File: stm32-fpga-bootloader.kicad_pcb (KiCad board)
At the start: 4 copper layers, 100 x 100 mm, 211 parts, among them J1 USB_C_Receptacle_USB2.0_14P, J10 LEDX, J1001 DATA, J1002 JTAG JUMP, J1003 JTAG-LOG, J1004 Conn_01x08, J11 LEDY, J12 PMOD, J13 Raspberry_Pi_2_3, J15 Conn_01x02, J3 RPI-TO-CPLD, J5 PMOD, J6 Conn_01x02, J7 TO-LCD, J8 USB_C_Receptacle_USB2.0_14P, J9 PMOD, Q1 2N7002K, Q2 2N7002K, Q3 2N7002K, Q4 2N7002K, Q5 2N7002K, Q6 2N7002K, Q7 2N7002K, SW1 BOOT, SW2 RUN, SW3 ICE_BTN, SW4 ICE_RST, SW5 BOOT, SW6 BTN, SW7 BTN, SW8 BTN, U1 AMS1117-3.3, U10 RP2040, U1001 XC6206PxxxMR, U11 74HC595D, U12 LTC-3743KD, U13 ACPL-798J-500E, U2 W25Q128JVS, U4 ACPL-798J-500E, U5 ICE40UP5K-SG48ITR, U6 W25Q128JVS, U7 LP5907MFX-1.2, U8 MAX7221xNG, U9 LCMXO2-1200HC-4TG100I, Y1 12Mhz

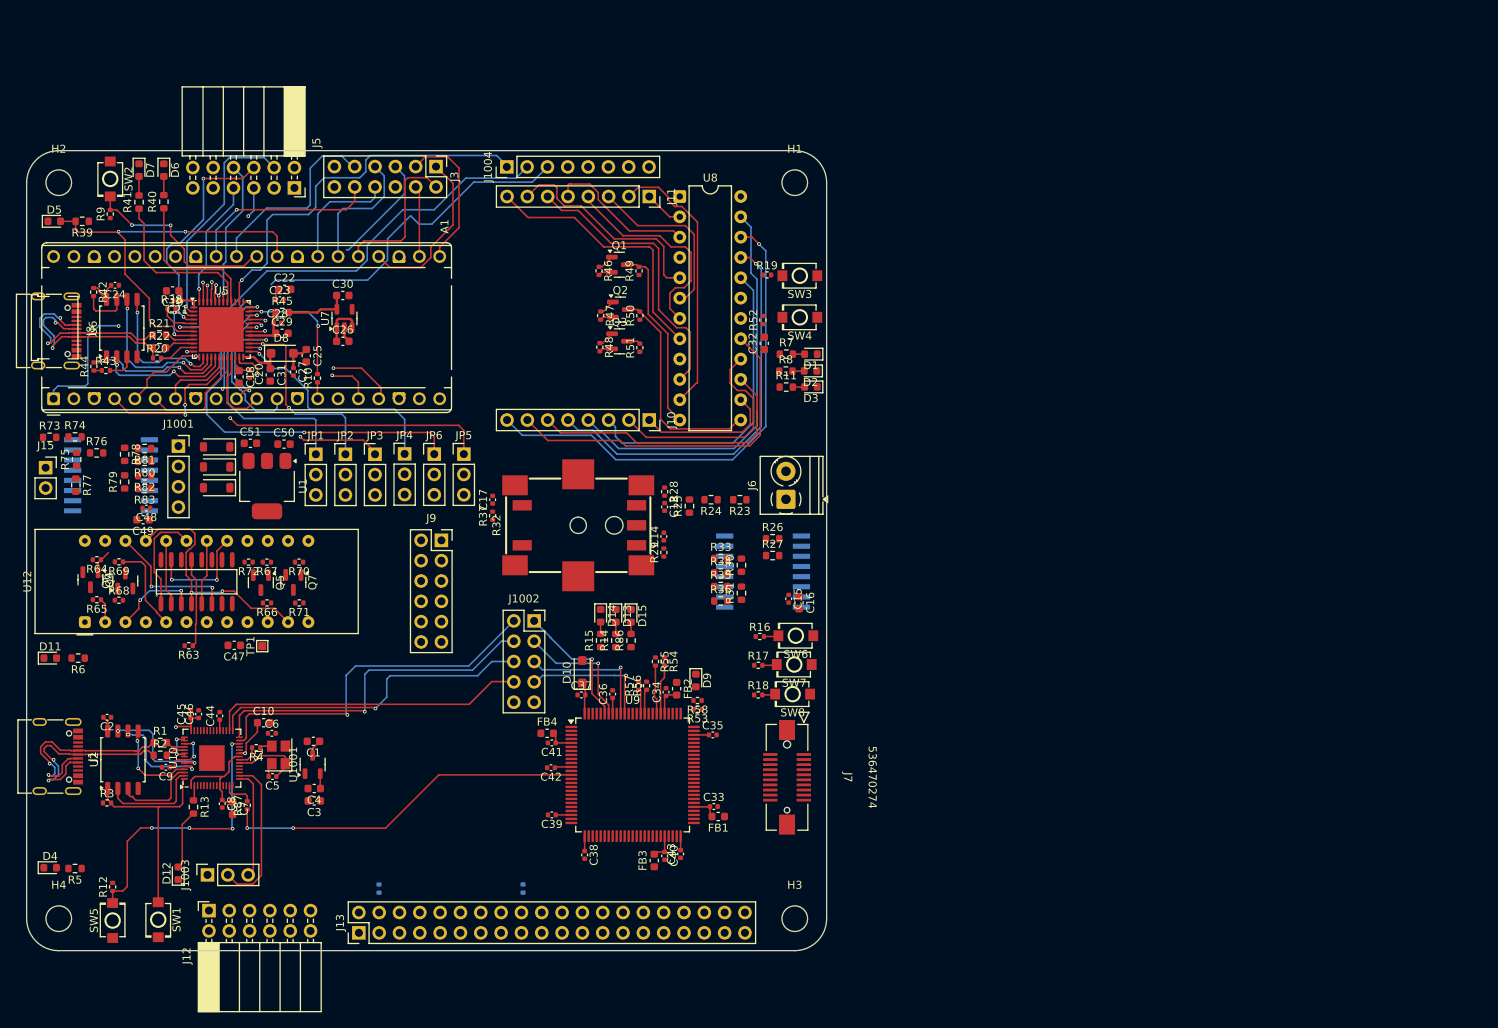
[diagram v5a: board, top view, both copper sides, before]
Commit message: Update the BOM and the routing
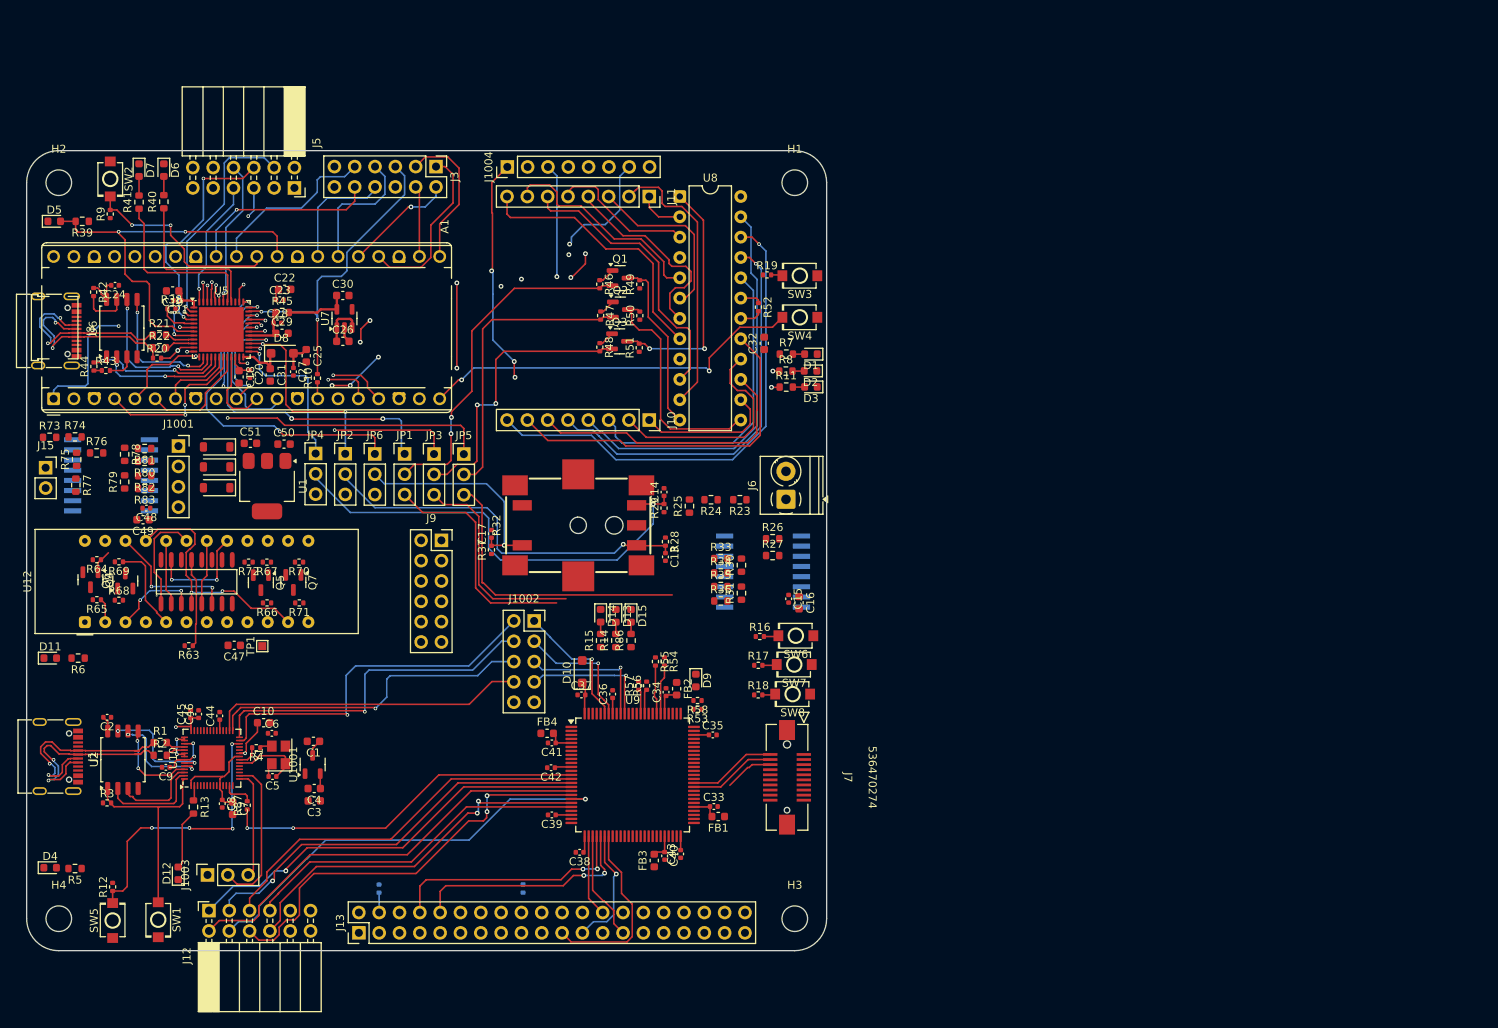
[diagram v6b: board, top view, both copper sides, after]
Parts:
- moved JP4 11.1 mm to (149.7, 68.0)
- moved JP1 11.1 mm to (160.8, 68.1)
- moved JP6 7.43 mm to (157.1, 68.1)
- moved JP3 7.38 mm to (164.5, 68.1)
- moved C13 6.25 mm to (193.4, 80.9)
- moved R28 6.25 mm to (193.4, 79.0)
- moved C14 5.56 mm to (193.2, 72.8)
- moved R29 5.56 mm to (193.2, 74.8)
- moved C17 4.27 mm to (171.7, 78.1)
- moved R37 4.27 mm to (171.7, 80.1)
- moved R52 1.71 mm to (205.0, 49.7), turned to -90 degrees
- moved R46 1.68 mm to (185.2, 46.9)
- moved Q1 1.68 mm to (187.7, 46.1)
- moved R49 1.68 mm to (190.2, 46.9)
- moved C38 0.70 mm to (182.7, 117.9), turned to 180 degrees
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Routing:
- net /LED1: track 0.00 -> 92.1 mm, vias 0 -> 3
- net /IOB_20a: track 4.64 -> 70.7 mm, vias 0 -> 4
- net /IOB_22a: track 0.86 -> 66.3 mm, vias 1 -> 2
- net /IOB_23b: track 10.5 -> 71.9 mm, vias 0 -> 5
- net /ENCODER_B: track 0.00 -> 58.0 mm, vias 0 -> 1
- net /IOT_43a: track 20.5 -> 77.6 mm, vias 1 -> 2
- net /lcmxo2-cpld-block/PL8D: track 0.00 -> 53.7 mm, vias 0 -> 1
- net /lcmxo2-cpld-block/PL8B: track 0.00 -> 53.2 mm
- net /lcmxo2-cpld-block/PL8C: track 0.00 -> 52.3 mm, vias 0 -> 2
- net /lcmxo2-cpld-block/PL8A: track 0.00 -> 51.8 mm, vias 0 -> 1
- net /lcmxo2-cpld-block/PL5D: track 0.00 -> 50.7 mm, vias 0 -> 1
- net /IOT_50b: track 48.8 -> 98.2 mm, vias 1 -> 5
- net /lcmxo2-cpld-block/PL5C: track 0.00 -> 48.6 mm
- net /ICE_nRST: track 5.61 -> 53.9 mm, vias 2 -> 4
- net /ENCODER_A: track 0.00 -> 48.1 mm, vias 0 -> 1
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
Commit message: Rework on pins assignements
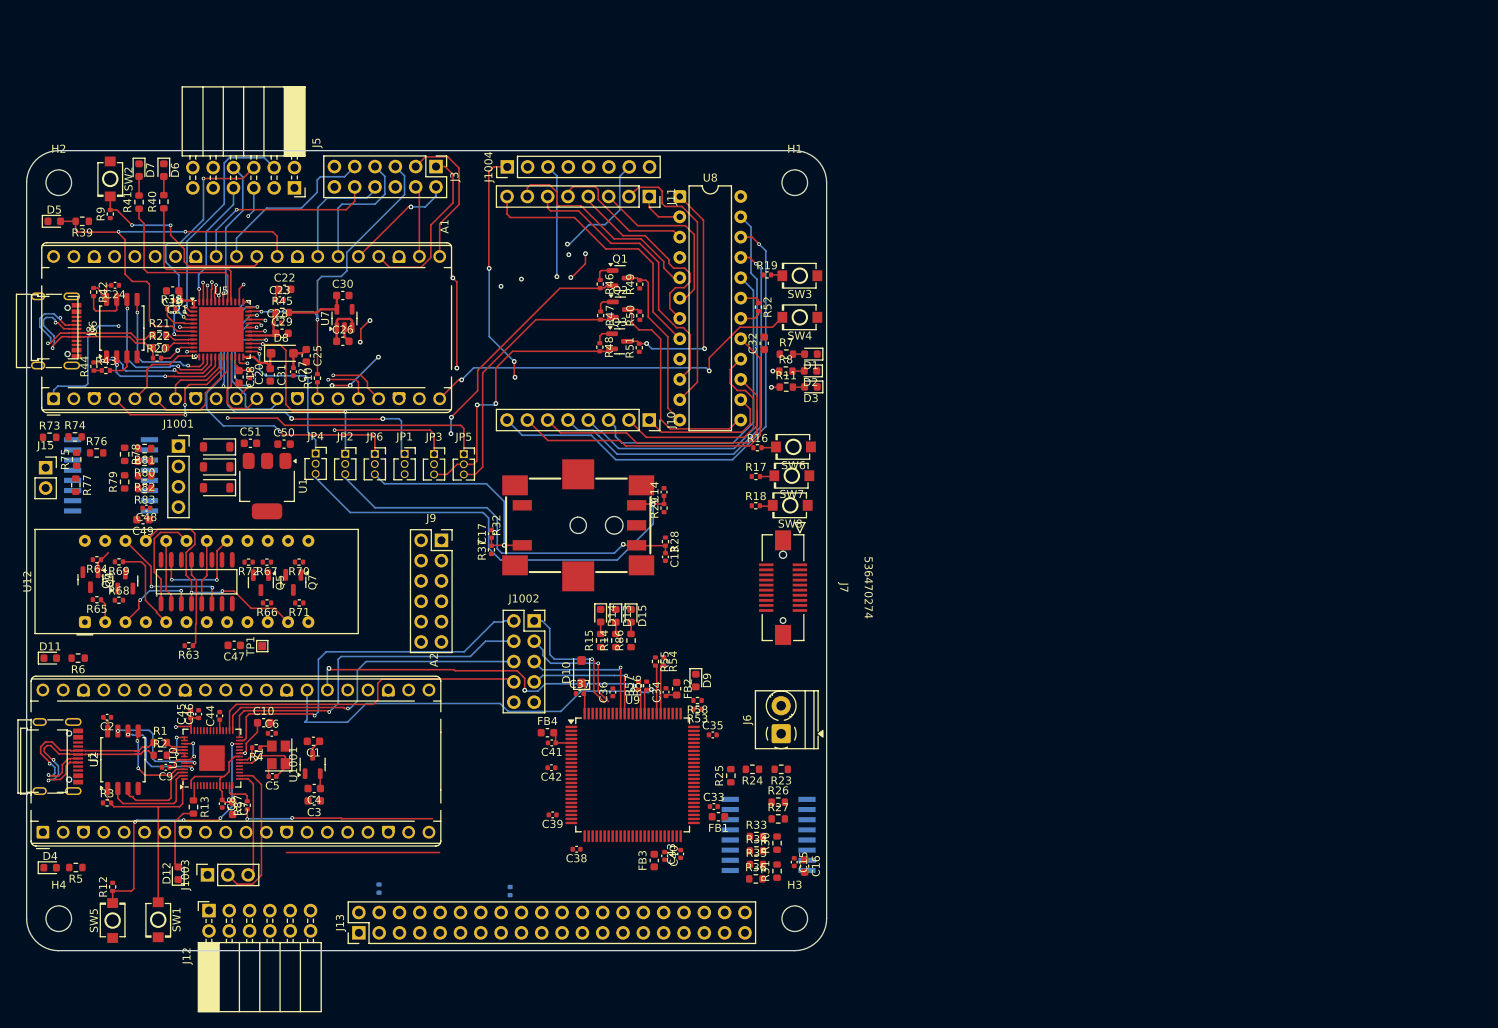
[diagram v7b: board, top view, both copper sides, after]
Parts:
- added A2: RaspberryPi_Pico, Module:RaspberryPi_Pico_Common_THT, F.Cu at (115.6, 115.3)
- JP1, JP2, JP3, JP4, JP5, JP6: footprint Connector_PinHeader_2.54mm:PinHeader_1x03_P2.54mm_Vertical -> Connector_PinSocket_1.27mm:PinSocket_1x03_P1.27mm_Vertical
- moved R33 35.0 mm to (204.8, 115.9)
- moved R34 35.0 mm to (204.8, 117.7)
- moved R35 35.0 mm to (204.8, 119.4)
- moved R30 35.0 mm to (207.4, 116.7)
- moved R31 35.0 mm to (207.4, 120.2)
- moved R36 35.0 mm to (204.7, 121.2)
- moved R24 34.1 mm to (204.3, 107.5)
- moved R25 34.1 mm to (201.6, 108.3)
- moved R23 34.1 mm to (207.9, 107.5)
- moved R27 32.9 mm to (207.5, 113.7)
- moved U4 32.9 mm to (206.3, 115.7)
- moved C15 32.9 mm to (209.5, 119.1)
- moved C16 32.9 mm to (210.8, 119.6)
- moved R26 32.9 mm to (207.5, 111.6)
- moved J6 29.3 mm to (207.9, 103.0)
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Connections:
- J1004 pad 1: /IOT_50b -> unconnected-(J1004-Pin_1-Pad1)
- J1004 pad 2: /IOB_13b -> unconnected-(J1004-Pin_2-Pad2)
- J1004 pad 3: /IOT_37a -> unconnected-(J1004-Pin_3-Pad3)
- J1004 pad 4: /IOB_20a -> unconnected-(J1004-Pin_4-Pad4)
- J1004 pad 5: /IOB_22a -> unconnected-(J1004-Pin_5-Pad5)
- J1004 pad 6: /IOB_23b -> unconnected-(J1004-Pin_6-Pad6)
- J1004 pad 7: /IOT_43a -> unconnected-(J1004-Pin_7-Pad7)
- J1004 pad 8: GND -> unconnected-(J1004-Pin_8-Pad8)
- J13 pad 11: /lcmxo2-cpld-block/PR5D/PCLKC1_0 -> unconnected-(J13-GPIO17-Pad11)
- J13 pad 12: /lcmxo2-cpld-block/PR5C/PCLKT1_0 -> unconnected-(J13-GPIO18/PWM0-Pad12)
- J13 pad 13: /lcmxo2-cpld-block/PR2A -> unconnected-(J13-GPIO27-Pad13)
- J13 pad 15: /lcmxo2-cpld-block/PR4B -> unconnected-(J13-GPIO22-Pad15)
- J13 pad 16: /lcmxo2-cpld-block/PR4A -> unconnected-(J13-GPIO23-Pad16)
- J13 pad 18: /lcmxo2-cpld-block/PR3B -> unconnected-(J13-GPIO24-Pad18)
- J13 pad 22: /lcmxo2-cpld-block/PR3A -> unconnected-(J13-GPIO25-Pad22)
- J13 pad 28: /lcmxo2-cpld-block/PT16C -> unconnected-(J13-ID_SC/GPIO1-Pad28)
- J13 pad 29: /lcmxo2-cpld-block/PT12A/PCLKT0_1 -> unconnected-(J13-GCLK1/GPIO5-Pad29)
- J13 pad 31: /lcmxo2-cpld-block/PT12B/PCLKC0_1 -> unconnected-(J13-GCLK2/GPIO6-Pad31)
- J13 pad 32: /lcmxo2-cpld-block/PT15A -> unconnected-(J13-PWM0/GPIO12-Pad32)
- J13 pad 35: /lcmxo2-cpld-block/PR5A -> unconnected-(J13-GPIO19/MISO1-Pad35)
- J13 pad 36: /lcmxo2-cpld-block/PR5B -> unconnected-(J13-GPIO16-Pad36)
- J13 pad 37: /lcmxo2-cpld-block/PR2B -> unconnected-(J13-GPIO26-Pad37)
- J13 pad 38: /lcmxo2-cpld-block/PR4D -> unconnected-(J13-GPIO20/MOSI1-Pad38)
- J13 pad 40: /lcmxo2-cpld-block/PR4C -> unconnected-(J13-GPIO21/SCLK1-Pad40)
- J13 pad 7: /lcmxo2-cpld-block/PT15B -> unconnected-(J13-GCLK0/GPIO4-Pad7)
- J7 pad 1: /PL4B -> /PR4C
- J7 pad 15: /PB11C -> /PR9D
- J7 pad 16: /PB9B/PCLKC2_0 -> /PR8C
- J7 pad 17: /PB9A/PCLKT2_0 -> /PR9B
- J7 pad 18: /PB11A/PCLKT2_1 -> /PR9A
- J7 pad 19: /PB11D -> /PR9C
- J7 pad 2: /PR8A -> /PR5A
- J7 pad 20: /PL4A -> /PR9B
- J7 pad 3: /PL10D -> /PR4D
- J7 pad 4: /PR8C -> /PR5B
- J7 pad 6: /PL10C -> /PR8A
- JP1 pad 3: /PR10C -> /PR3B
- JP2 pad 3: /PB15A -> /PR2A
- JP3 pad 3: /PR8D -> /PR4A
- JP4 pad 3: /PB15B -> /PR2B
- JP5 pad 3: /PR10D -> /PR4B
- JP6 pad 3: /PB11B/PCLKC2_1 -> /PR3A
- R16 pad 2: /lcmxo2-cpld-block/PL2D/L_GPLLC_IN -> /lcmxo2-cpld-block/PT15A
- R17 pad 2: /lcmxo2-cpld-block/PL2C/L_GPLLT_IN -> /lcmxo2-cpld-block/PT16C
- R18 pad 2: /lcmxo2-cpld-block/PL3A/PCLKT3_2 -> /lcmxo2-cpld-block/PT15B
- SW6 pad 2: /lcmxo2-cpld-block/PL2D/L_GPLLC_IN -> /lcmxo2-cpld-block/PT15A
- SW7 pad 2: /lcmxo2-cpld-block/PL2C/L_GPLLT_IN -> /lcmxo2-cpld-block/PT16C
- SW8 pad 2: /lcmxo2-cpld-block/PL3A/PCLKT3_2 -> /lcmxo2-cpld-block/PT15B
- U9 pad 53: /CPLD_B7_PR9D -> /PR9D
- U9 pad 54: /CPLD_B6_PR9C -> /PR9C
- U9 pad 57: /CPLD_B5_PR9B -> /PR9B
- U9 pad 58: /CPLD_B4_PR9A -> /PR9A
- U9 pad 62: /lcmxo2-cpld-block/PR5D/PCLKC1_0 -> /PR5D/PCLKC1_0
- U9 pad 63: /lcmxo2-cpld-block/PR5C/PCLKT1_0 -> /PR5C/PCLKT1_0
- U9 pad 64: /lcmxo2-cpld-block/PR5B -> /PR5B
- U9 pad 65: /lcmxo2-cpld-block/PR5A -> /PR5A
- U9 pad 66: /lcmxo2-cpld-block/PR4D -> /PR4D
- U9 pad 67: /lcmxo2-cpld-block/PR4C -> /PR4C
- U9 pad 68: /lcmxo2-cpld-block/PR4B -> /PR4B
- U9 pad 69: /lcmxo2-cpld-block/PR4A -> /PR4A
- U9 pad 70: /lcmxo2-cpld-block/PR3B -> /PR3B
- U9 pad 71: /lcmxo2-cpld-block/PR3A -> /PR3A
- U9 pad 74: /lcmxo2-cpld-block/PR2B -> /PR2B
- U9 pad 75: /lcmxo2-cpld-block/PR2A -> /PR2A
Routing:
- net /lcmxo2-cpld-block/PL8D: track 53.7 -> 0.00 mm, vias 1 -> 0
- net /lcmxo2-cpld-block/PL8B: track 53.2 -> 0.00 mm
- net /lcmxo2-cpld-block/PL8C: track 52.3 -> 0.00 mm, vias 2 -> 0
- net /lcmxo2-cpld-block/PL8A: track 51.8 -> 0.00 mm, vias 1 -> 0
- net /lcmxo2-cpld-block/PL5D: track 50.7 -> 0.00 mm, vias 1 -> 0
- net /CPLD_SCL: track 3.08 -> 51.5 mm, vias 0 -> 1
- net /CPLD_SDA: track 3.08 -> 49.9 mm, vias 0 -> 3
- net /lcmxo2-cpld-block/PL9A/PCLKT3_0: track 46.6 -> 0.00 mm, vias 2 -> 0
- net /lcmxo2-cpld-block/PL9B/PCLKC3_0: track 43.7 -> 0.00 mm
- net /PR10D: track 36.9 -> 0.00 mm
- net /lcmxo2-cpld-block/PB6A: track 30.5 -> 0.00 mm, vias 2 -> 0
- net /lcmxo2-cpld-block/PL5C: track 48.6 -> 19.2 mm
- net /PR10C: track 29.4 -> 0.00 mm
- net /lcmxo2-cpld-block/PB6B: track 29.0 -> 0.00 mm, vias 2 -> 0
- net /PR8D: track 26.9 -> 0.00 mm
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
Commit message: Rework on pins assignements
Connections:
- A2 pad 10: /CPLD_B7_PR9D -> /CPLD_B7_PL3B/PCLKC3_2
- A2 pad 6: /CPLD_B4_PR9A -> /CPLD_B4_PL2C/L_GPLLT_IN
- A2 pad 7: /CPLD_B5_PR9B -> /CPLD_B5_PL2D/L_GPLLC_IN
- A2 pad 9: /CPLD_B6_PR9C -> /CPLD_B6_PL3A/PCLKT3_2
- U9 pad 1: /lcmxo2-cpld-block/PL2C/L_GPLLT_IN -> /CPLD_B4_PL2C/L_GPLLT_IN
- U9 pad 10: /PL4B -> unconnected-(U9-PL4B-Pad10)
- U9 pad 2: /lcmxo2-cpld-block/PL2D/L_GPLLC_IN -> /CPLD_B5_PL2D/L_GPLLC_IN
- U9 pad 24: /PL10D -> unconnected-(U9-PL10C-Pad24)
- U9 pad 25: /PL10C -> unconnected-(U9-PL10D-Pad25)
- U9 pad 3: /lcmxo2-cpld-block/PL3A/PCLKT3_2 -> /CPLD_B6_PL3A/PCLKT3_2
- U9 pad 34: /PB9A/PCLKT2_0 -> unconnected-(U9-PB9A/PCLKT2_0-Pad34)
- U9 pad 35: /PB9B/PCLKC2_0 -> unconnected-(U9-PB9B/PCLKC2_0-Pad35)
- U9 pad 36: /PB11C -> unconnected-(U9-PB11C-Pad36)
- U9 pad 37: /PB11D -> unconnected-(U9-PB11D-Pad37)
- U9 pad 38: /PB11A/PCLKT2_1 -> unconnected-(U9-PB11A/PCLKT2_1-Pad38)
- U9 pad 39: /PB11B/PCLKC2_1 -> unconnected-(U9-PB11B/PCLKC2_1-Pad39)
- U9 pad 4: /lcmxo2-cpld-block/PL3B/PCLKC3_2 -> /CPLD_B7_PL3B/PCLKC3_2
- U9 pad 40: /PB15A -> unconnected-(U9-PB15A-Pad40)
- U9 pad 41: /PB15B -> unconnected-(U9-PB15B-Pad41)
- U9 pad 51: /PR10D -> unconnected-(U9-PR10D-Pad51)
- U9 pad 52: /PR10C -> unconnected-(U9-PR10C-Pad52)
- U9 pad 59: /PR8D -> unconnected-(U9-PR8D-Pad59)
- U9 pad 62: /PR5D/PCLKC1_0 -> unconnected-(U9-PR5D/PCLKC1_0-Pad62)
- U9 pad 63: /PR5C/PCLKT1_0 -> unconnected-(U9-PR5C/PCLKT1_0-Pad63)
- U9 pad 9: /PL4A -> unconnected-(U9-PL4A-Pad9)
